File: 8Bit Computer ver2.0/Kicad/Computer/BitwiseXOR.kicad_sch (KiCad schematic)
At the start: 5 parts, among them IC17 SN74LVC1G14DBVR, IC18 SN74HCS86DR, IC19 SN74HCS74DR, IC20 SN74HCS86DR, IC21 SN74HCS574DGSR

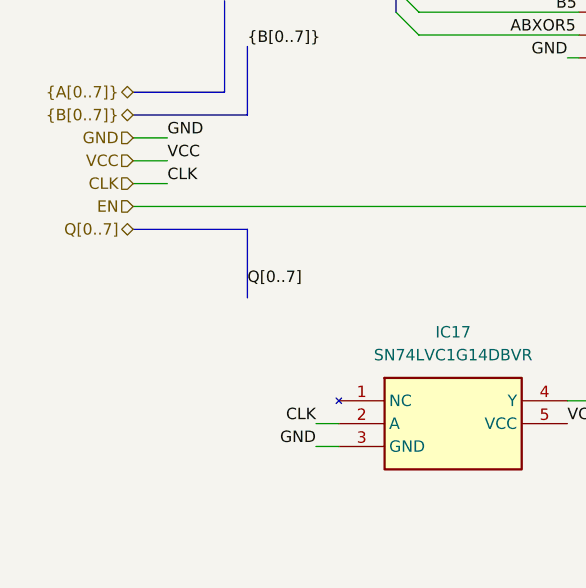
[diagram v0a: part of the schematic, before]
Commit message: Kicad,parts
Kicad:
added FlagRegister
began Inc, Comp
parts:
added comparator for P>Q 682
added faster sram 12ns AS7C
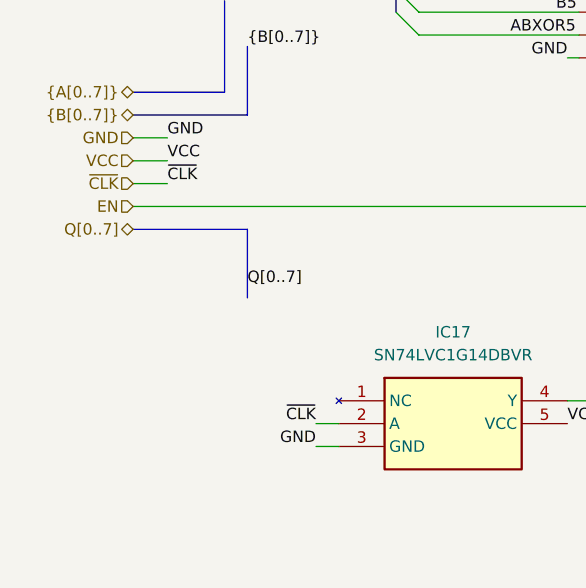
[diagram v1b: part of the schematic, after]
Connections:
- net CLK renamed ~{CLK}
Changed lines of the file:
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@@
 		)
 	)
-	(label "CLK"
+	(label "~{CLK}"
 		(at 67.31 125.73 180)
 		(effects
@@
 		)
 	)
-	(label "CLK"
+	(label "~{CLK}"
 		(at 50.8 99.06 0)
 		(effects
@@
 		)
 	)
-	(hierarchical_label "CLK"
+	(hierarchical_label "~{CLK}"
 		(shape input)
 		(at 46.99 99.06 180)

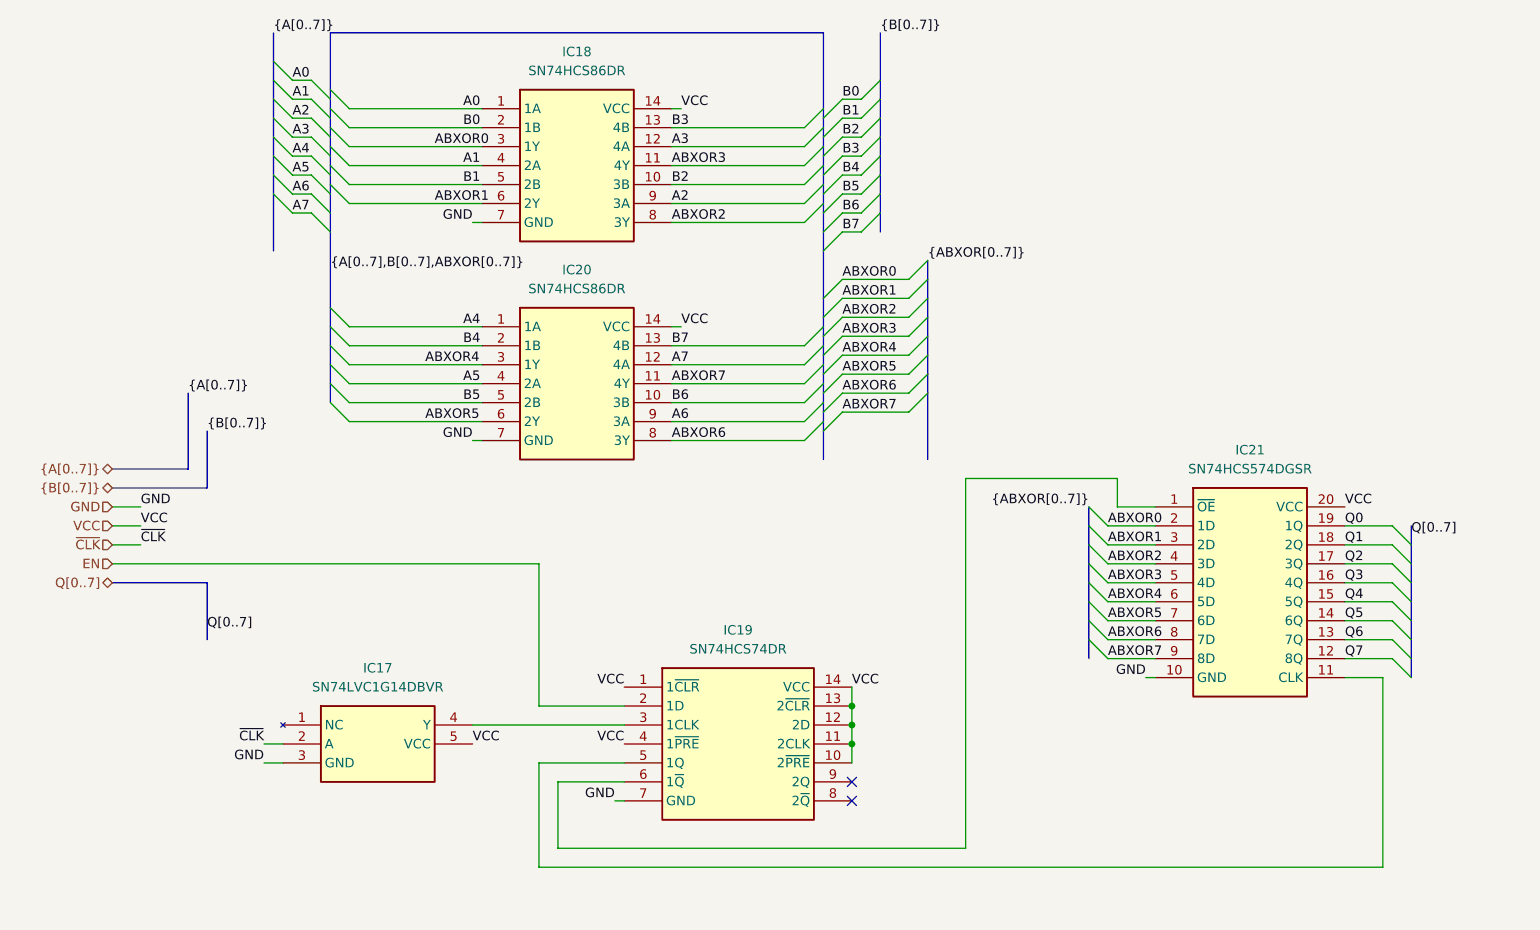
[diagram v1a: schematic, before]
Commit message: parts,Kicad
parts:
changed 8xDlatch HCS to ABT 574
waiting for SRAM CAD Model
Kicad:
imported AHC types of ICs
added ProgrammeCounter
finished Comparator
changed all HCS to AHC except 3in OR ->no AHC Version
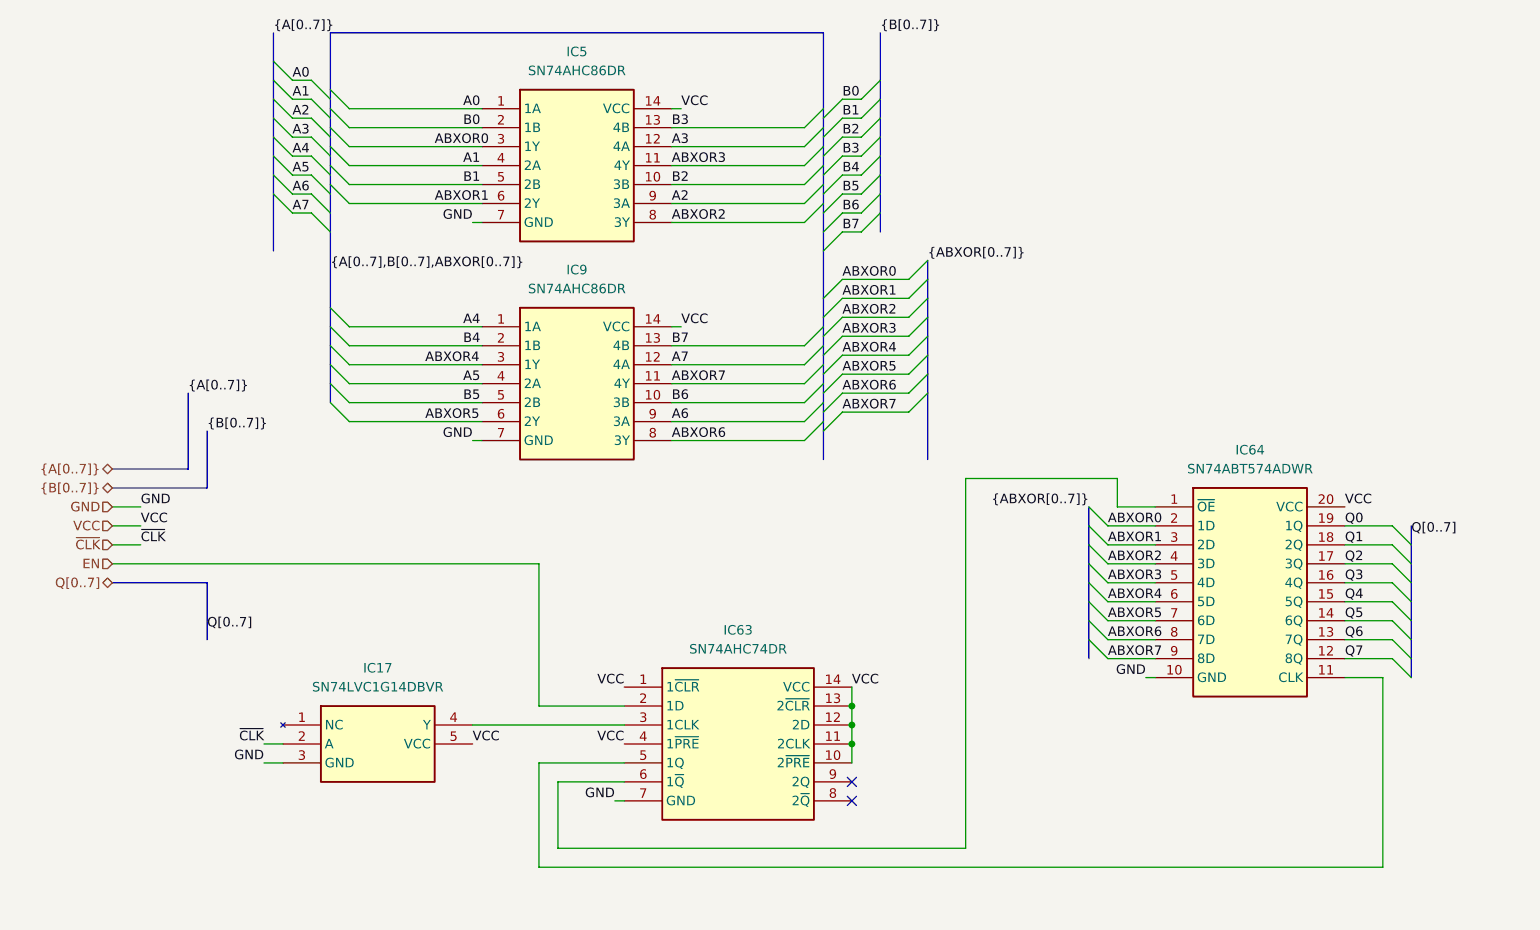
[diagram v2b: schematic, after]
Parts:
- removed IC18, IC20: SN74HCS86DR, Samacsys:SOIC127P600X175-14N, symbol Samacsys:SN74HCS86DR
- removed IC19: SN74HCS74DR, Samacsys:SOIC127P600X175-14N, symbol Samacsys:SN74HCS74DR
- removed IC21: SN74HCS574DGSR, Samacsys:SOP50P490X110-20N, symbol Samacsys:SN74HCS574DGSR
- added IC5, IC9: SN74AHC86DR, Samacsys:SOIC127P600X175-14N, symbol Samacsys:SN74AHC86DR
- added IC63: SN74AHC74DR, Samacsys:SOIC127P600X175-14N, symbol Samacsys:SN74AHC74DR
- added IC64: SN74ABT574ADWR, Samacsys:SOIC127P1030X265-20N, symbol Samacsys:SN74ABT574ADWR
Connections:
- net A0: now also IC5.1 (1A)
- net A1: now also IC5.4 (2A)
- net A2: now also IC5.9 (3A)
- net A3: now also IC5.12 (4A)
- net A4: now also IC9.1 (1A)
- net A5: now also IC9.4 (2A)
- net A6: now also IC9.9 (3A)
- net A7: now also IC9.12 (4A)
- net ABXOR0: now also IC5.3 (1Y), IC64.2 (1D)
- net ABXOR1: now also IC5.6 (2Y), IC64.3 (2D)
- net ABXOR2: now also IC5.8 (3Y), IC64.4 (3D)
- net ABXOR3: now also IC5.11 (4Y), IC64.5 (4D)
- net ABXOR4: now also IC64.6 (5D), IC9.3 (1Y)
- net ABXOR5: now also IC64.7 (6D), IC9.6 (2Y)
- net ABXOR6: now also IC64.8 (7D), IC9.8 (3Y)
- net ABXOR7: now also IC64.9 (8D), IC9.11 (4Y)
- net B0: now also IC5.2 (1B)
- net B1: now also IC5.5 (2B)
- net B2: now also IC5.10 (3B)
- net B3: now also IC5.13 (4B)
- net B4: now also IC9.2 (1B)
- net B5: now also IC9.5 (2B)
- net B6: now also IC9.10 (3B)
- net B7: now also IC9.13 (4B)
- net EN: now also IC63.2 (1D)
- net GND: now also IC5.7 (GND), IC63.7 (GND), IC64.10 (GND), IC9.7 (GND)
- net Q0: now also IC64.19 (1Q)
- net Q1: now also IC64.18 (2Q)
- net Q2: now also IC64.17 (3Q)
- net Q3: now also IC64.16 (4Q)
- net Q4: now also IC64.15 (5Q)
- net Q5: now also IC64.14 (6Q)
- net Q6: now also IC64.13 (7Q)
- net Q7: now also IC64.12 (8Q)
- net VCC: now also IC5.14 (VCC), IC63.1 (1~{CLR}), IC63.10 (2~{PRE}), IC63.11 (2CLK), IC63.12 (2D), IC63.13 (2~{CLR}), IC63.14 (VCC), IC63.4 (1~{PRE}), IC64.20 (VCC), IC9.14 (VCC)
- net at IC17.4 (Y): now also IC63.3 (1CLK)
- new net: IC63.5 (1Q), IC64.11 (CLK)
- new net: IC63.6 (1~{Q}), IC64.1 (~{OE})

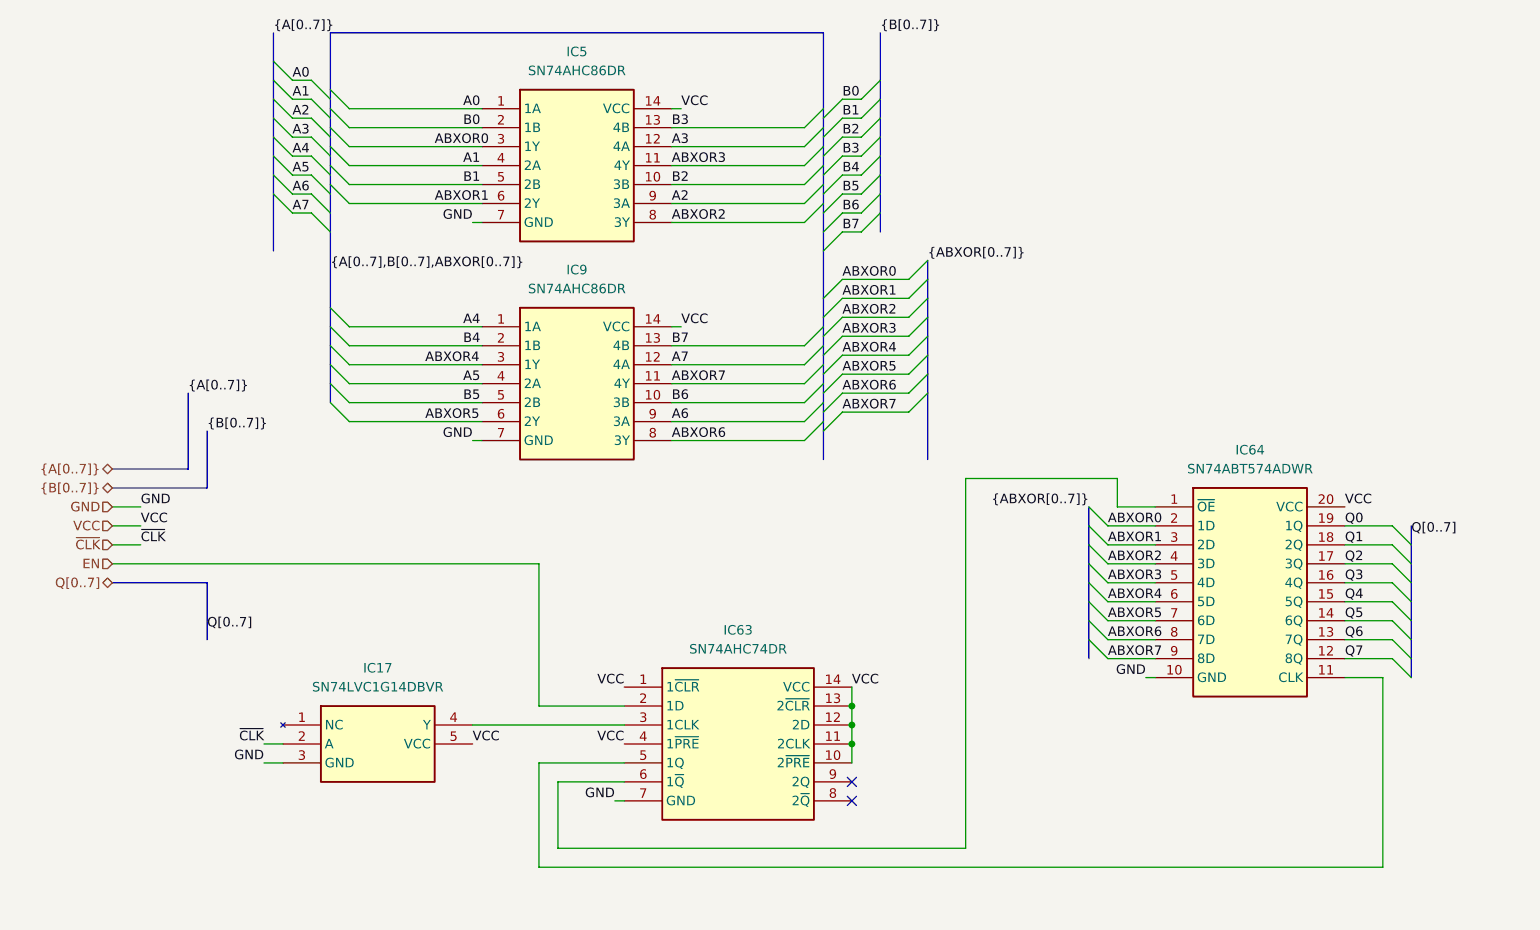
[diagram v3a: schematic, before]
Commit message: Kicad, parts
Parts:
added Leds
Kicad:
added Input Output
changed Q bus to DAT bus
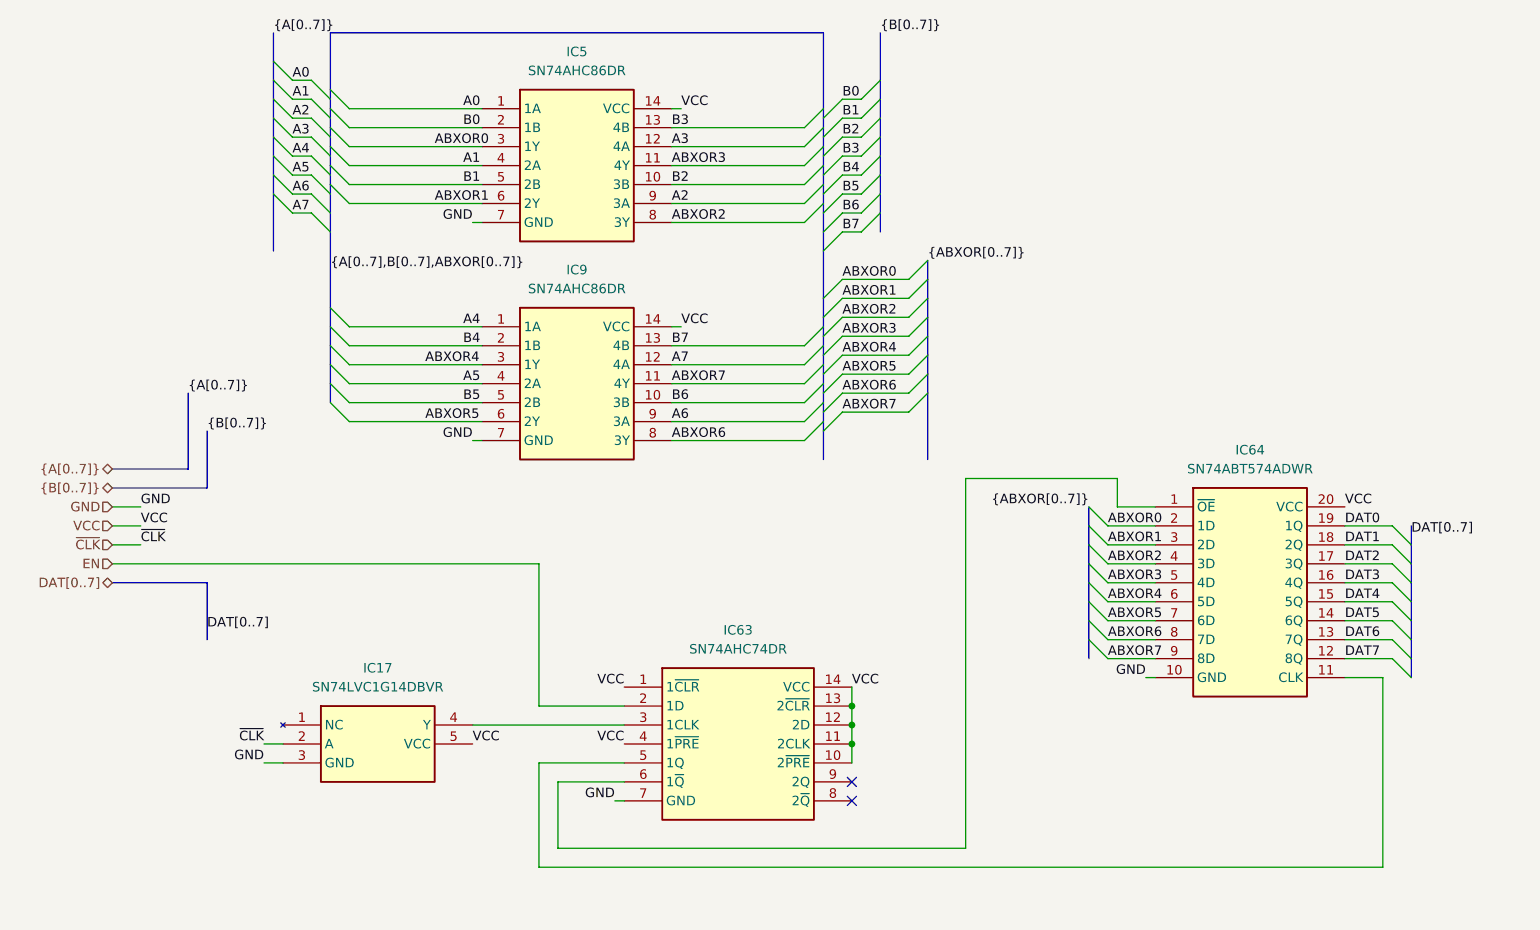
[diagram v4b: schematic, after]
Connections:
- net Q0 renamed DAT0
- net Q1 renamed DAT1
- net Q2 renamed DAT2
- net Q3 renamed DAT3
- net Q4 renamed DAT4
- net Q5 renamed DAT5
- net Q6 renamed DAT6
- net Q7 renamed DAT7
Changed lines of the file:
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@@
 		)
 	)
-	(label "Q4"
+	(label "DAT4"
 		(at 212.09 106.68 0)
 		(effects
@@
 		)
 	)
-	(label "Q[0..7]"
+	(label "DAT[0..7]"
 		(at 59.69 110.49 0)
 		(effects
@@
 		)
 	)
-	(label "Q0"
+	(label "DAT0"
 		(at 212.09 96.52 0)
 		(effects
@@
 		)
 	)
-	(label "Q1"
+	(label "DAT1"
 		(at 212.09 99.06 0)
 		(effects
@@
 		)
 	)
-	(label "Q5"
+	(label "DAT5"
 		(at 212.09 109.22 0)
 		(effects
@@
 		)
 	)
-	(label "Q3"
+	(label "DAT3"
 		(at 212.09 104.14 0)
 		(effects
@@
 		)
 	)
-	(label "Q6"
+	(label "DAT6"
 		(at 212.09 111.76 0)
 		(effects
@@
 		)
 	)
-	(label "Q7"
+	(label "DAT7"
 		(at 212.09 114.3 0)
 		(effects
@@
 		)
 	)
-	(label "Q2"
+	(label "DAT2"
 		(at 212.09 101.6 0)
 		(effects
@@
 		)
 	)
-	(label "Q[0..7]"
+	(label "DAT[0..7]"
 		(at 220.98 97.79 0)
 		(effects
@@
 		)
 	)
-	(hierarchical_label "Q[0..7]"
+	(hierarchical_label "DAT[0..7]"
 		(shape tri_state)
 		(at 46.99 104.14 180)

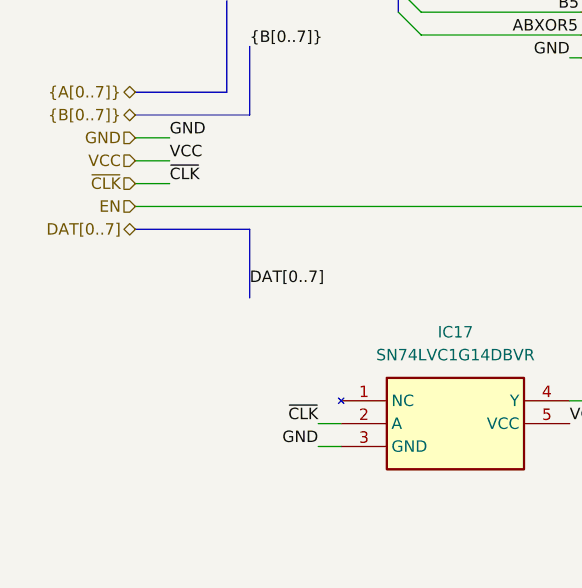
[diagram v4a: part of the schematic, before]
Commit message: Kicad, parts
parts:
added USB C PD Triggerboard
added Delay Chip for 90ns
added Push Button
Kicad:
added USB C PD Triggerboard
added rising edge detector via Delay and Xor for Accept Push Button
added VBUS net
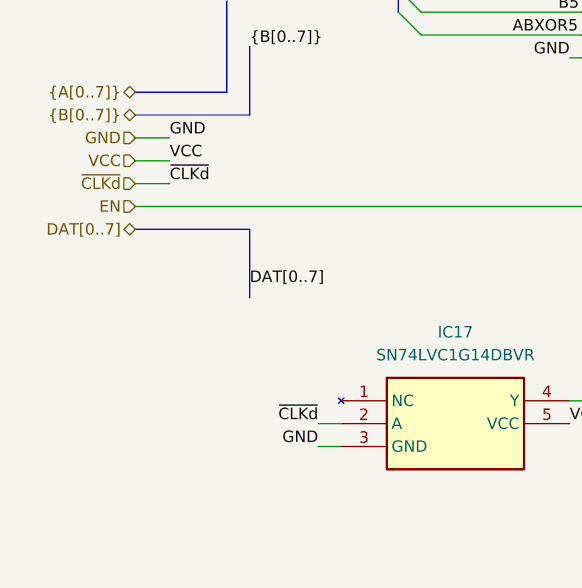
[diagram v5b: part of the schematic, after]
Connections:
- net ~{CLK} renamed ~{CLKd}
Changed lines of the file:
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@@
 		)
 	)
-	(label "~{CLK}"
+	(label "~{CLKd}"
 		(at 67.31 125.73 180)
 		(effects
@@
 		)
 	)
-	(label "~{CLK}"
+	(label "~{CLKd}"
 		(at 50.8 99.06 0)
 		(effects
@@
 		)
 	)
-	(hierarchical_label "~{CLK}"
+	(hierarchical_label "~{CLKd}"
 		(shape input)
 		(at 46.99 99.06 180)
